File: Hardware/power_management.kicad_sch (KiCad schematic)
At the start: 38 parts, among them J2 Conn_01x03, SW27 SW_DPDT_x2, U2 BQ24040, U3 BQ51050BRHL, U4 AP22814BW5, U5 TPS2116DRL

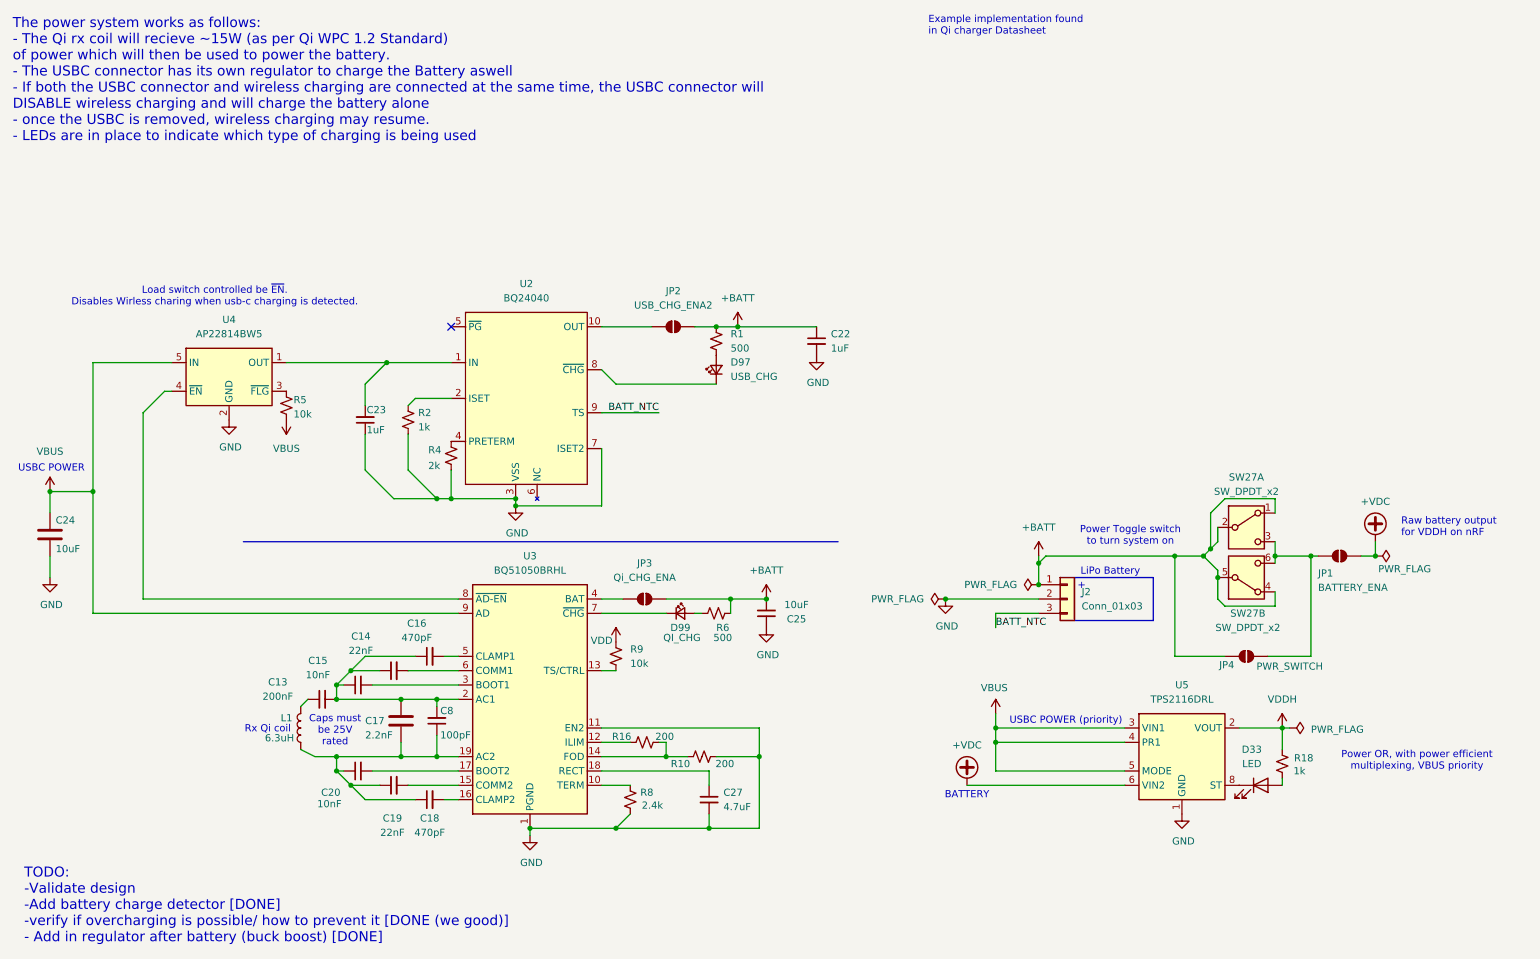
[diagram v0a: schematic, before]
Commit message: added mounting holes
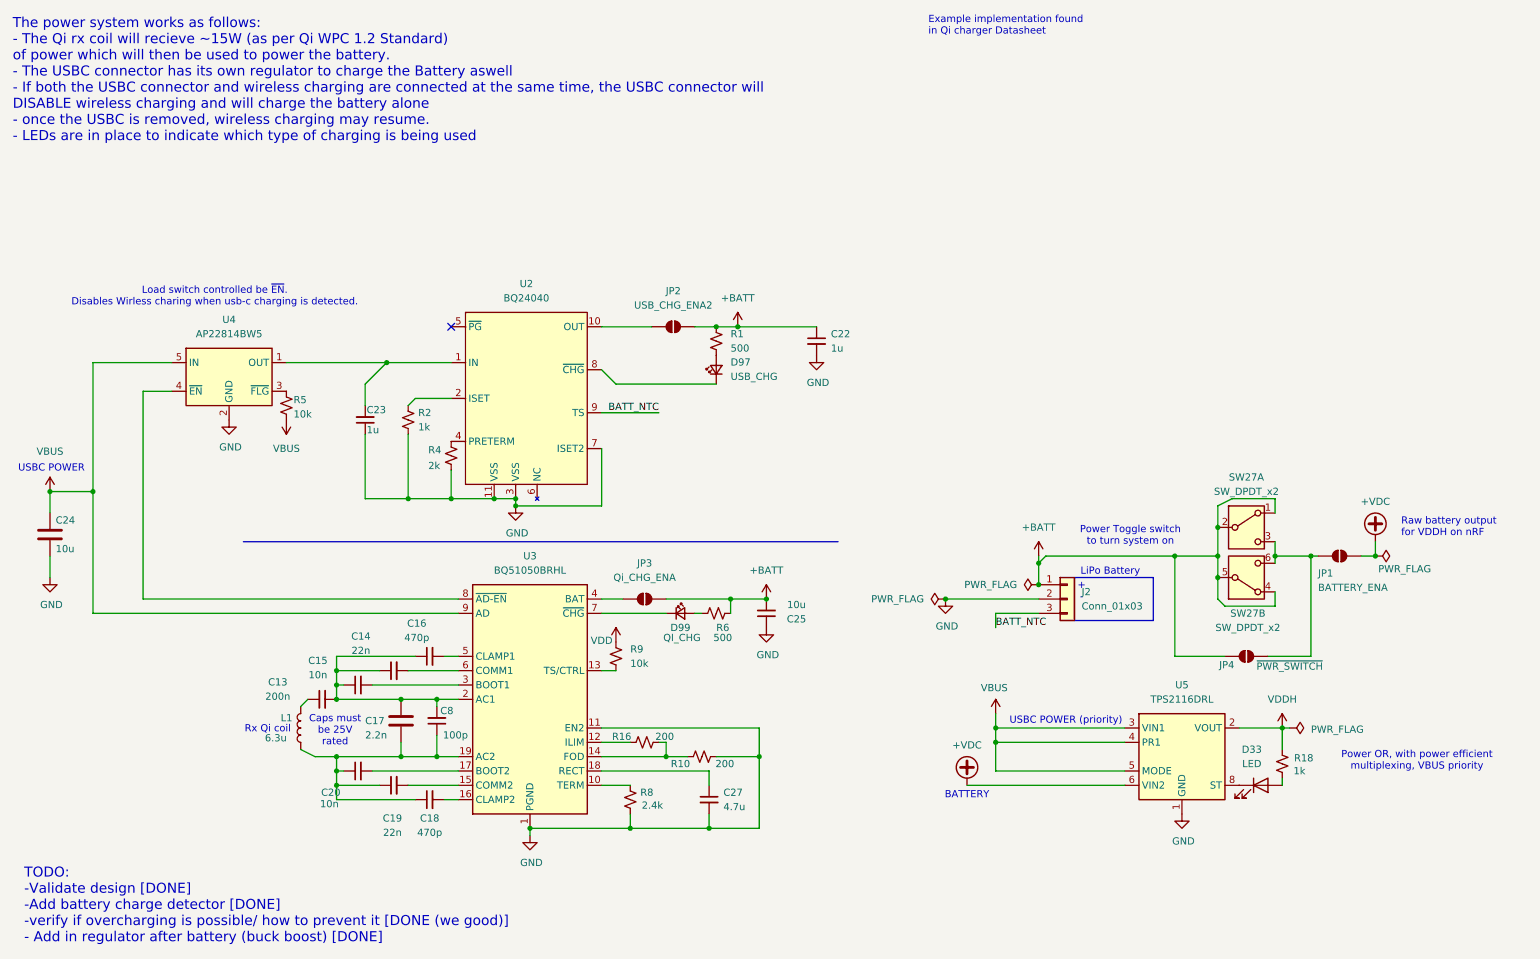
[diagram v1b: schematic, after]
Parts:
- C13: value 200nF -> 200n
- C14, C19: value 22nF -> 22n
- C15, C20: value 10nF -> 10n
- C16, C18: value 470pF -> 470p
- C17: value 2.2nF -> 2.2n
- C22, C23: value 1uF -> 1u
- C24, C25: value 10uF -> 10u
- C27: value 4.7uF -> 4.7u
- C8: value 100pF -> 100p
- JP4: value PWR_SWITCH -> ~{PWR_SWITCH}
- L1: value 6.3uH -> 6.3u
- U2: LCSC (none) -> C2876332
- U3: LCSC (none) -> C133307
- U5: LCSC (none) -> C3235557
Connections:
- net GND: now also U2.11 (VSS)
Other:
- note added: "TODO: -Validate design [DONE] -Add battery charge detector [DONE] -verify if overcharging is possible/ how to prevent it [DONE (we good)] - Add in regulator after battery (buck boost) [DONE]"
- note removed: "TODO: -Validate design -Add battery charge detector [DONE] -verify if overcharging is possible/ how to prevent it [DONE (we good)] - Add in regulator after battery (buck boost) [DONE]"

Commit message: Add LCSC part numbers and new resistor to PCB
Added LCSC part numbers to multiple components in hornet_kb.kicad_pcb for improved BOM generation. Introduced a new 500Ω resistor (R11) and updated net assignments for Q1 and D27. Modified .gitignore to exclude backup and auto-save files, and removed obsolete backup files from Hardware/hornet_kb-backups. Made symbol and footprint tweaks in Custom_sym.kicad_sym.
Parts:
- removed U4: AP22814BW5, Package_TO_SOT_SMD:SOT-23-5, symbol Power_Management:AP22814BW5
- added Q1: BTS4140N, Package_TO_SOT_SMD:SOT-223, symbol Transistor_FET_Other:BTS4140N
- D33: LCSC (none) -> C28310436
- D97, D99: LCSC (none) -> C20608784
- J2: LCSC (none) -> C514175
- L1: footprint Connector_JST:JST_EH_S2B-EH_1x02_P2.50mm_Horizontal -> TerminalBlock_Phoenix:TerminalBlock_Phoenix_MKDS-1,5-2-5.08_1x02_P5.08mm_Horizontal; LCSC (none) -> C8465
- SW27: LCSC (none) -> C1788494
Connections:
- net VBUS: now also R5.2, Q1.2 (V_{bb}), Q1.4 (V_{bb}); no longer R5.1
- net at C23.2, U2.1 (IN): now also Q1.3 (OUT)
- net at U3.8 (~{AD-EN}): now also R5.1, Q1.1 (IN)

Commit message: Added LCSC part defs
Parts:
- C13: LCSC (none) -> C1002
- C14, C19: LCSC (none) -> C21122
- C15, C20: LCSC (none) -> C57112
- C16, C18: LCSC (none) -> C1620
- C17: LCSC (none) -> C1604
- C22, C23: LCSC (none) -> C15849
- C24, C25: LCSC (none) -> C19702
- C27: LCSC (none) -> C19666
- C8: LCSC (none) -> C14858
- R1, R6: LCSC (none) -> C6207671
- R10, R16: LCSC (none) -> C8218
- R18, R2: LCSC (none) -> C21190
- R4: LCSC (none) -> C22975
- R5, R9: LCSC (none) -> C25804
- R8: LCSC (none) -> C22940
